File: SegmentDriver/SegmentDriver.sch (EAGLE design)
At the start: 220 parts, among them IC1 ATMEGA644A, IC2 PCA9555PW, IC3 4511D, K1 691313710002, K10 M02-MOLEX-104188-0210, K11 M02-MOLEX-104188-0210, K12 M02-MOLEX-104188-0210, K13 M02-MOLEX-104188-0210, K14 M02-MOLEX-104188-0210, K15 M02-MOLEX-104188-0210, K16 M02-MOLEX-104188-0210, K17 691210910004, K18 691210910004, K19 691210910004, K2 691313710002, K20 691210910004, K21 691210910004, K22 691210910004, K23 691210910004, K24 691210910004, K25 691210910004, K3 691322310002, K4 691322310002, K6 61200621621, K7 61201021621, K8 M02-MOLEX-104188-0210, K9 M02-MOLEX-104188-0210, Q1 MOSFET-NCHANNEL-FDMS5672, Q2 MOSFET-NCHANNEL-FDMS5672, Q3 MOSFET-NCHANNEL-FDMS5672, Q4 MOSFET-NCHANNEL-FDMS5672, Q5 MOSFET-NCHANNEL-FDMS5672, Q6 MOSFET-NCHANNEL-FDMS5672, Q7 MOSFET-NCHANNEL-FDMS5672, Q8 MOSFET-NCHANNEL-FDMS5672, Q9 MOSFET-NCHANNEL-FDMS5672, SW1 SPST_TACT-EVQQ2, U1 DS1307SO8-TIGHT, U10 FOD8321, U11 FOD8321, U15 DMP2215L-7, U16 DMP2215L-7, U3 FOD8321, U4 FOD8321, U5 FOD8321, U6 FOD8321, U7 FOD8321, U8 FOD8321, U9 FOD8321, X1 53261-03, X2 53261-03, X3 53261-03, X4 53261-03, X5 53261-03, X6 53261-03, Y2 32.768kHz

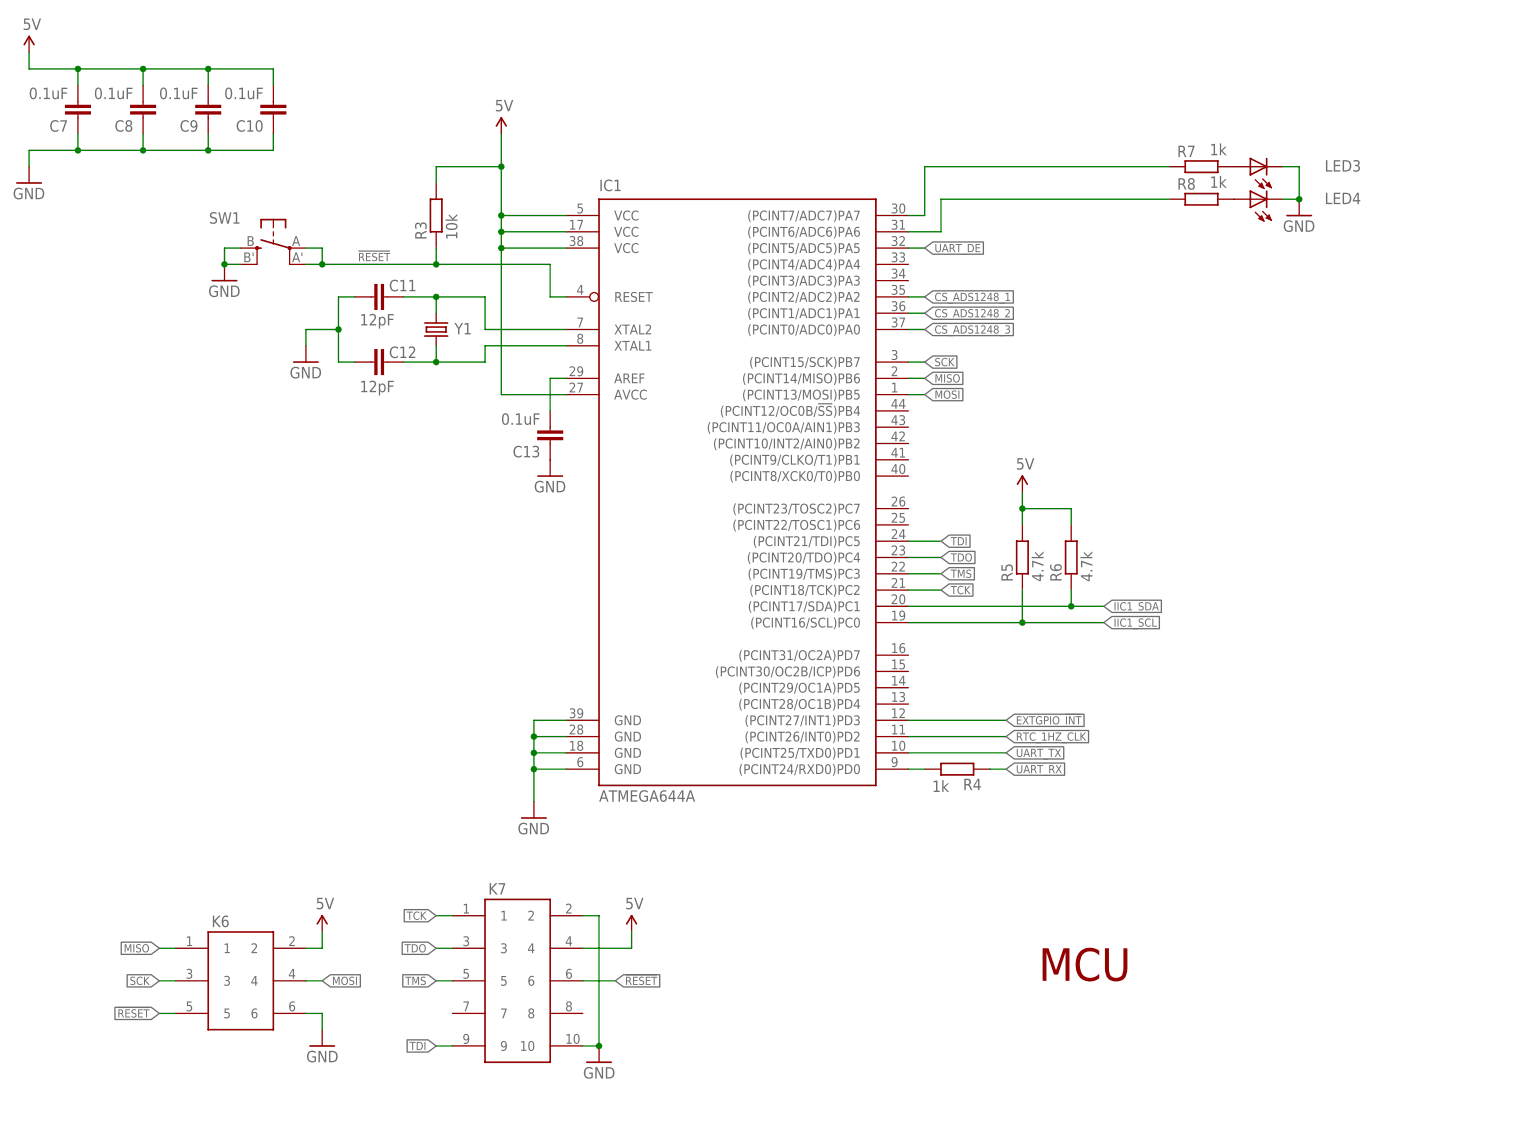
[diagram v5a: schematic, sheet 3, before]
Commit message: added power rails
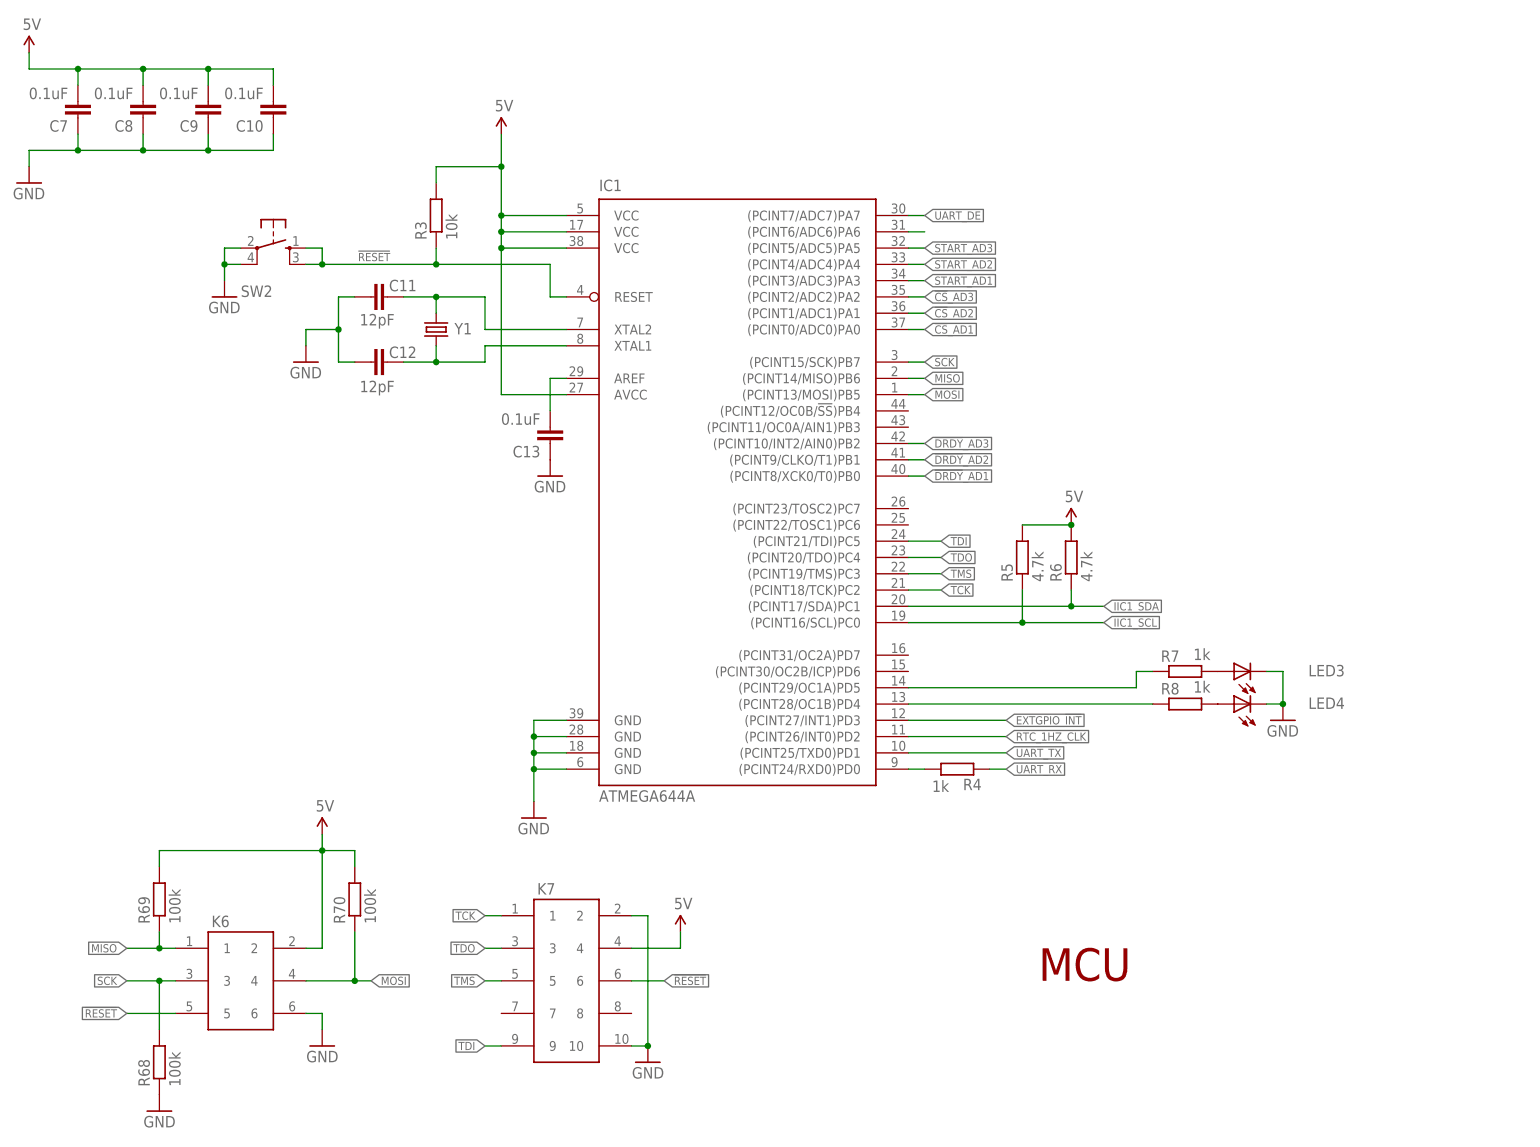
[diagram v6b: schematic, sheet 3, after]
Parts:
- removed SW1: SPST_TACT-EVQQ2, adafruit:SPST_TACT-EVQQ2
- added C81, C84: 4.7uF, rcl:C-EUC0603K
- added C82, C83, C85: 4.7uF, rcl:C-EUC0805K
- added R62, R63, R64, R65, R66, R67, R68, R69, R70: 100k, rcl:R-EU_R0603
- added SW2: (no value), simbits:434153017835_FIXED
- added U18: 7808, simbits:78XXKTTR-D2PACK
- added U19: ADP3333ARM-5, simbits:ADP3333ARM-5
- added U20: 7805, simbits:78XXKTTR-D2PACK
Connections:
- removed net +12V: C15.1, C16.1, C17.1, C18.1, C19.1, C2.1, C20.1, C21.1, C22.1, C23.1, C4.1, C6.2, K3.1, K4.2, R2.2, U10.VDD@6, U11.VDD@6, U3.VDD@6, U4.VDD@6, U5.VDD@6, U6.VDD@6, U7.VDD@6, U8.VDD@6, U9.VDD@6
- removed net AVDD: C36.1, C37.1, C38.1, U12.AVDD@22, U13.AVDD@22, U14.AVDD@22
- removed net CS_ADS1248_1: IC1.(PCINT2/ADC2)PA2
- removed net CS_ADS1248_2: IC1.(PCINT1/ADC1)PA1
- removed net CS_ADS1248_3: IC1.(PCINT0/ADC0)PA0
- removed net DVDD: C33.1, C34.1, C35.1, R19.2, R20.2, R21.2, U12.DVDD@1, U13.DVDD@1, U14.DVDD@1
- removed net N$83: IC2.I/O0.3, R58.4
- removed net N$84: IC2.I/O0.4, R59.1
- removed net N$85: IC2.I/O0.5, R59.2
- removed net N$86: IC2.I/O0.6, R59.3
- removed net N$87: IC2.I/O0.7, R59.4
- new net !ADCSUP_SD: U19.!SD!@7
- new net +15V: C15.1, C16.1, C17.1, C18.1, C19.1, C2.1, C20.1, C21.1, C22.1, C23.1, C4.1, C6.2, K3.1, K4.2, R2.2, U10.VDD@6, U11.VDD@6, U18.VI, U3.VDD@6, U4.VDD@6, U5.VDD@6, U6.VDD@6, U7.VDD@6, U8.VDD@6, U9.VDD@6
- new net +8V: C82.2, C83.2, C85.2, U18.VO, U19.IN@2, U20.VI
- new net ADC_5V: C33.1, C34.1, C35.1, C36.1, C37.1, C38.1, C81.2, R19.2, R20.2, R21.2, R62.2, R63.2, R64.2, R65.2, R66.2, R67.2, U12.AVDD@22, U12.DVDD@1, U13.AVDD@22, U13.DVDD@1, U14.AVDD@22, U14.DVDD@1, U19.OUT@1
- new net N$30: IC2.I/O0.0, R58.4
- new net N$41: IC2.I/O0.4, R59.4
- new net N$53: IC2.I/O0.5, R59.3
- new net N$54: IC2.I/O0.6, R59.2
- new net N$55: IC2.I/O0.7, R59.1
- new net N$58: IC1.(PCINT6/ADC6)PA6
- net !CS!_AD1: now also IC1.(PCINT0/ADC0)PA0, R63.1
- net !CS!_AD2: now also IC1.(PCINT1/ADC1)PA1, R64.1
- net !CS!_AD3: now also IC1.(PCINT2/ADC2)PA2, R66.1
- net !DRDY!_AD1: now also IC1.(PCINT8/XCK0/T0)PB0, R62.1
- net !DRDY!_AD2: now also IC1.(PCINT9/CLKO/T1)PB1, R65.1
- net !DRDY!_AD3: now also IC1.(PCINT10/INT2/AIN0)PB2, R67.1
- net !RESET: now also SW2.1, SW2.3; no longer SW1.P, SW1.P1
- net +5V: now also C84.2, U20.VO
- net 5V: now also R69.2, R70.2
- net GND: now also C81.1, C82.1, C83.1, C84.1, C85.1, R68.1, SW2.2, SW2.4, U18.GND, U19.GND@3, U19.NC@4..6,8, U20.GND; no longer SW1.S, SW1.S1
- net GPIO1: now also R58.5; no longer R58.8
- net GPIO2: now also R58.6; no longer R58.7
- net GPIO3: now also R58.7; no longer R58.6
- net GPIO4: now also R58.8; no longer R58.5
- net GPIO5: now also R59.5; no longer R59.8
- net GPIO6: now also R59.6; no longer R59.7
- net GPIO7: now also R59.7; no longer R59.6
- net GPIO8: now also R59.8; no longer R59.5
- net LED1: now also IC1.(PCINT29/OC1A)PD5; no longer IC1.(PCINT7/ADC7)PA7
- net LED2: now also IC1.(PCINT28/OC1B)PD4; no longer IC1.(PCINT6/ADC6)PA6
- net MISO: now also R69.1
- net MOSI: now also R70.1
- net N$36: now also IC2.I/O0.1, R58.3; no longer IC2.I/O0.0, R58.1
- net N$37: now also IC2.I/O0.2; no longer IC2.I/O0.1
- net N$38: now also IC2.I/O0.3, R58.1; no longer IC2.I/O0.2, R58.3
- net SCK: now also R68.2
- net START_AD1: now also IC1.(PCINT3/ADC3)PA3
- net START_AD2: now also IC1.(PCINT4/ADC4)PA4
- net START_AD3: now also IC1.(PCINT5/ADC5)PA5
- net UART_DE: now also IC1.(PCINT7/ADC7)PA7; no longer IC1.(PCINT5/ADC5)PA5
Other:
- moved on the sheet: C4, C6, K7, LED2, LED3, LED4, R19, R2, R20, R21, R58, R59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

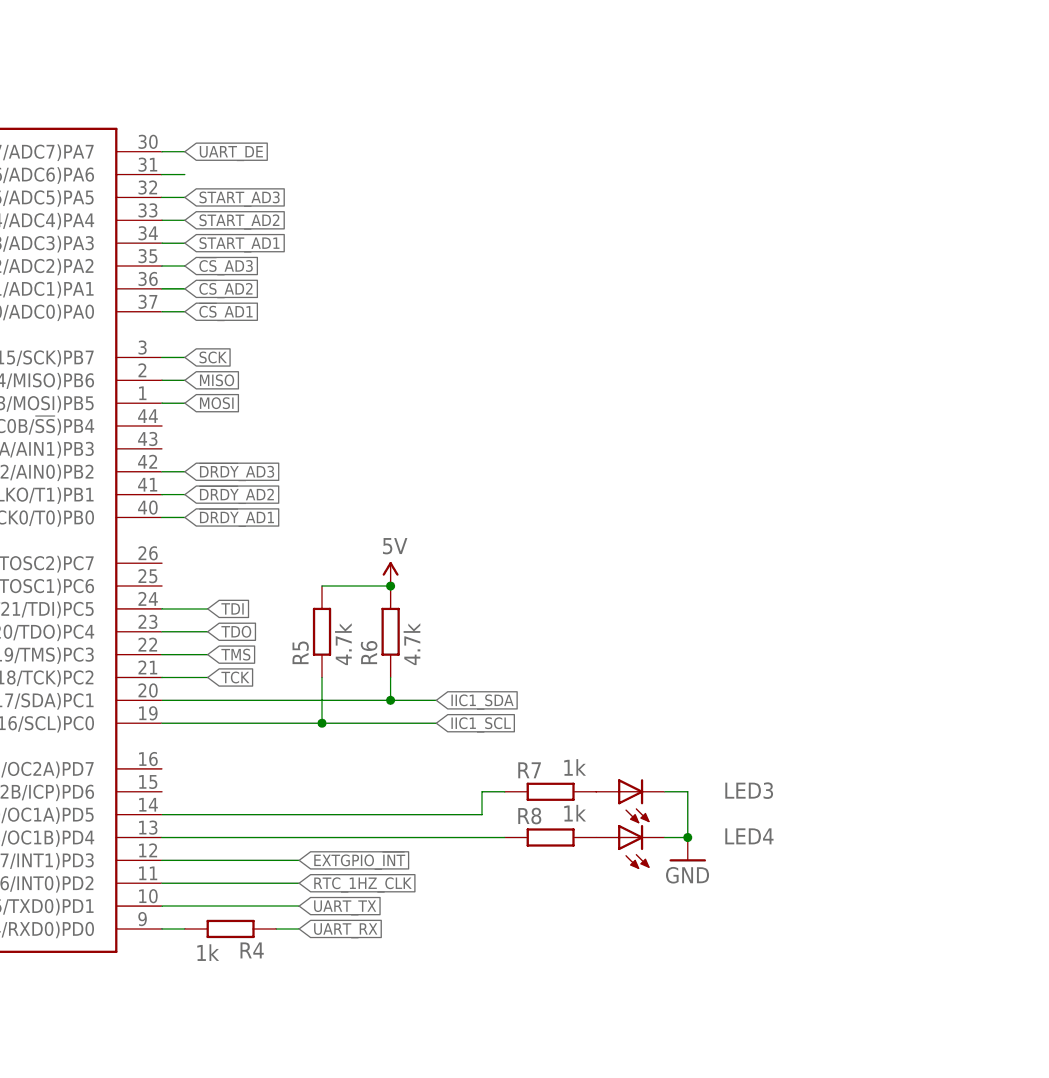
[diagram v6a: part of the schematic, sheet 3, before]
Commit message: gpio connections
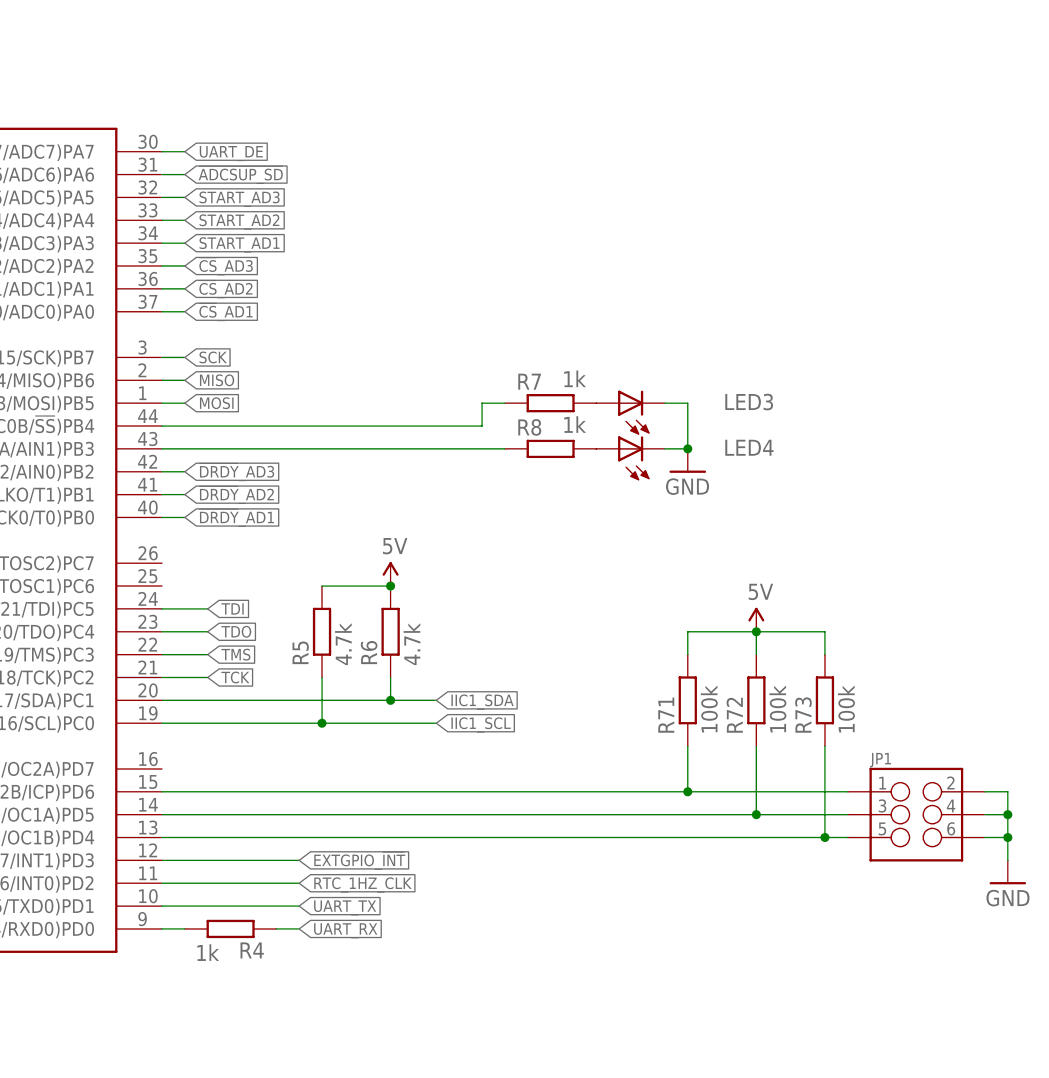
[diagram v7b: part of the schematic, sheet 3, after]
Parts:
- added JP1: (no value), SparkFun-Connectors:M03X22X3_SILK_SM
- added R71, R72, R73: 100k, rcl:R-EU_R0603
- added R74, R75: 10k, rcl:R-EU_R0603
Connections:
- net GPIO1 renamed GPIO0.0
- net GPIO2 renamed GPIO0.1
- net GPIO3 renamed GPIO0.2
- net GPIO4 renamed GPIO0.3
- net GPIO5 renamed GPIO0.4
- net GPIO6 renamed GPIO0.5
- removed net GPIO7: R59.7
- removed net GPIO8: R59.8
- removed net LED2: IC1.(PCINT28/OC1B)PD4, R8.1
- removed net N$64: U17.RE
- new net GPIO0.6_OUT: K5.B4, R59.7
- new net GPIO0.7_OUT: K5.B7, R59.8
- new net GPIO1.6_IN: IC2.I/O1.6, K5.A4, R74.1
- new net GPIO1.7_IN: IC2.I/O1.7, K5.A7, R75.1
- new net N$56: IC1.(PCINT28/OC1B)PD4, JP1.5, R73.1
- new net N$57: IC1.(PCINT29/OC1A)PD5, JP1.3, R72.1
- new net N$59: IC1.(PCINT11/OC0A/AIN1)PB3, R8.1
- net !ADCSUP_SD: now also IC1.(PCINT6/ADC6)PA6
- net +5V: now also R74.2, R75.2
- net 5V: now also R71.2, R72.2, R73.2
- net GND: now also JP1.2, JP1.4, JP1.6, K5.A5, K5.A6, K5.A8, K5.B5, K5.B6, K5.B8, U17.RE
- net LED1: now also IC1.(PCINT12/OC0B/!SS!)PB4; no longer IC1.(PCINT29/OC1A)PD5
- net N$58: now also IC1.(PCINT30/OC2B/ICP)PD6, JP1.1, R71.1; no longer IC1.(PCINT6/ADC6)PA6
- net RS485+: now also K5.B2; no longer K5.B1
- net RS485-: now also K5.B1; no longer K5.B2
- net RTC_1HZ_CLK: now also K5.A3, K5.B3
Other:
- moved on the sheet: LED3, LED4, R7, R8

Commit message: schematics finished (probably)
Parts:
- added C86, C87, C88, C89, C90, C91: 1uF, rcl:C-EUC0603K
- added R76, R77: 120, rcl:R-EU_R0603
- added R78, R80, R82, R84, R86, R88: 69k, rcl:R-EU_R0603
- added R79, R81, R83, R85, R87, R89: 18k, rcl:R-EU_R0603
- added SW1, SW3, SW4, SW5, SW6, SW7: (no value), simbits:434153017835_FIXED
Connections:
- new net GPIO6_OUT: K5.B4, R76.2
- new net GPIO7_OUT: K5.B7, R77.2
- new net N$64: R78.2, R79.2, SW1.1, SW1.3, X1-2.S
- new net N$66: R80.2, R81.2, SW3.1, SW3.3, X2-2.S
- new net N$68: R82.2, R83.2, SW4.1, SW4.3, X3-2.S
- new net N$70: R84.2, R85.2, SW5.1, SW5.3, X4-2.S
- new net N$72: R86.2, R87.2, SW6.1, SW6.3, X5-2.S
- new net N$79: R88.2, R89.2, SW7.1, SW7.3, X6-2.S
- net +5V: now also R78.1, R80.1, R82.1, R84.1, R86.1, R88.1
- net AGND: now also C1.2, C3.2, C5.1, K1.2, K2.1, LED1.C, U10.VSS@4, U11.VSS@4, U3.VSS@4, U4.VSS@4, U5.VSS@4, U6.VSS@4, U7.VSS@4, U8.VSS@4, U9.VSS@4
- net GND: now also C86.1, C87.1, C88.1, C89.1, C90.1, C91.1, SW1.2, SW1.4, SW3.2, SW3.4, SW4.2, SW4.4, SW5.2, SW5.4, SW6.2, SW6.4, SW7.2, SW7.4; no longer C1.2, C3.2, C5.1, K1.2, K2.1, LED1.C, U10.VSS@4, U11.VSS@4, U3.VSS@4, U4.VSS@4, U5.VSS@4, U6.VSS@4, U7.VSS@4, U8.VSS@4, U9.VSS@4
- net GPIO0.0: now also C86.2, R79.1; no longer X1-2.S
- net GPIO0.1: now also C87.2, R81.1; no longer X2-2.S
- net GPIO0.2: now also C88.2, R83.1; no longer X3-2.S
- net GPIO0.3: now also C89.2, R85.1; no longer X4-2.S
- net GPIO0.4: now also C90.2, R87.1; no longer X5-2.S
- net GPIO0.5: now also C91.2, R89.1; no longer X6-2.S
- net GPIO0.6_OUT: now also R76.1; no longer K5.B4
- net GPIO0.7_OUT: now also R77.1; no longer K5.B7
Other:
- moved on the sheet: X1-1, X1-2, X1-3, X2-1, X2-2, X2-3, X3-1, X3-2, X3-3, X4-1, X4-2, X4-3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
